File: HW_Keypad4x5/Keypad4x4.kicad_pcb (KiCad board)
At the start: 2 copper layers, 76 x 133 mm, 81 parts, among them J1 USB_C_Receptacle_USB2.0, J2 Conn_01x04, J3 Conn_01x05, J4 L_Power, J5 R_Power, J6 L_Comm, J7 R_Comm, SW1 SW_Push, SW10 SW_Push, SW11 SW_Push, SW12 SW_Push, SW13 SW_Push, SW14 SW_Push, SW15 SW_Push, SW16 SW_Push, SW17 SW_Push, SW18 SW_Push, SW19 SW_Push, SW2 SW_Push, SW20 SW_Push, SW3 SW_Push, SW4 SW_Push, SW5 SW_Push, SW6 SW_Push, SW7 SW_Push, SW8 SW_Push, SW9 SW_Push, U1 LM1117-3.3, U2 STM32F407VGTx, U3 USBLC6-2SC6, Y1 25Mhz

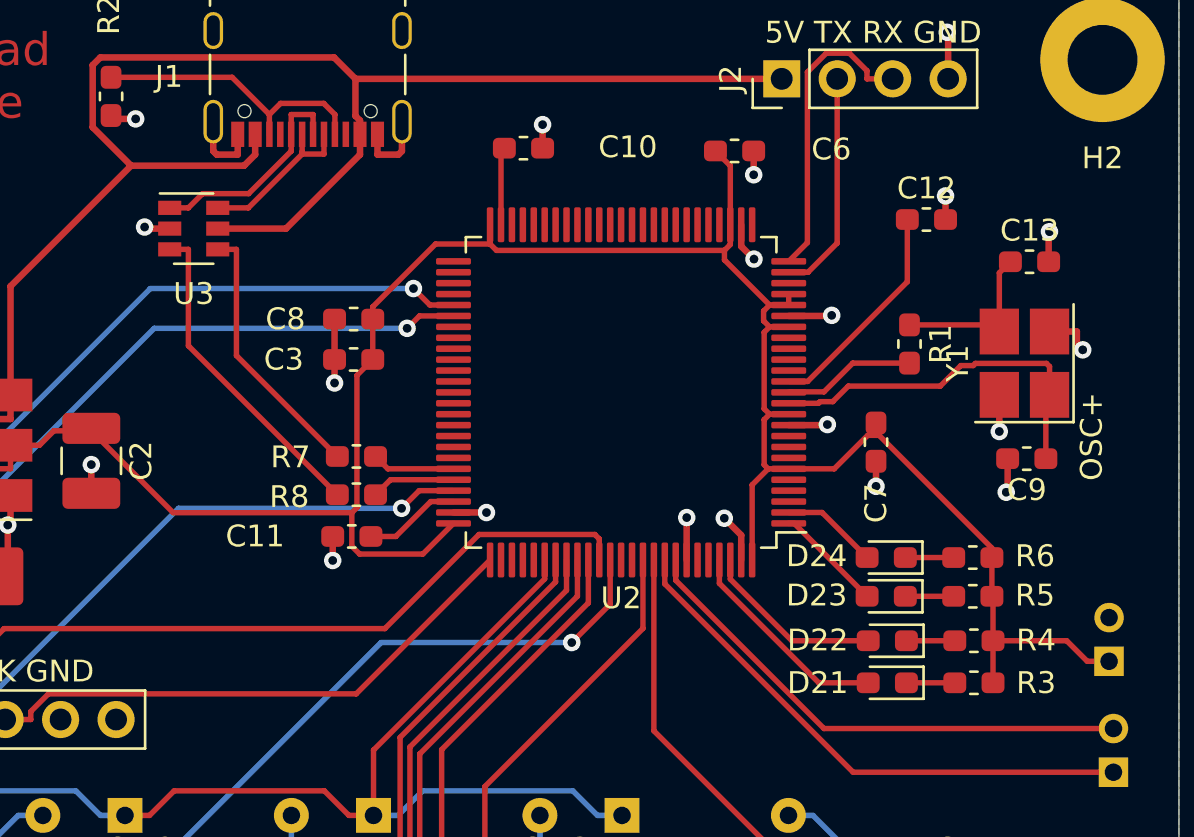
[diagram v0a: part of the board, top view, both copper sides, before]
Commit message: Fix Error USBLC6-2SC6
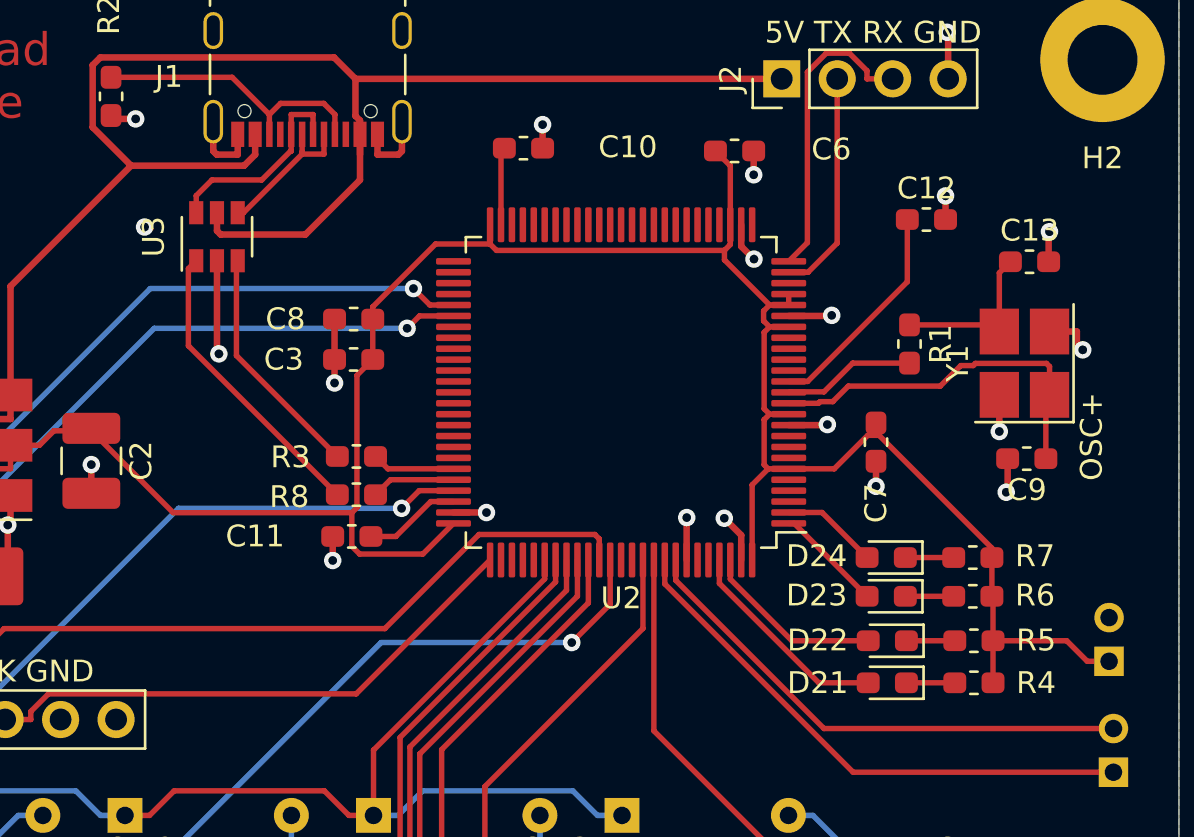
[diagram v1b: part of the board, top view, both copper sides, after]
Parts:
- moved U3 1.13 mm to (41.5, -16.9), turned to 90 degrees
- renumbered J7 to J6, J6 to J7, R7 to R3, R3 to R4, R4 to R5, R5 to R6, R6 to R7
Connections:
- U3 pad 1: /USB_CONN_P -> /USBDM+
- U3 pad 3: /USBDM+ -> /USBDM-
- U3 pad 4: /USBDM- -> /USB_CONN_N
- U3 pad 6: /USB_CONN_N -> /USB_CONN_P
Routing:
- net GND: track 46.2 -> 49.6 mm, vias 22 -> 23
- net +5VD: track 78.8 -> 81.4 mm
- net /USBDM-: track 12.3 -> 10.9 mm
- net /USBDM+: track 14.9 -> 13.7 mm
- net /USB_CONN_N: track 7.69 -> 6.87 mm
- net /USB_CONN_P: track 10.2 -> 9.55 mm
